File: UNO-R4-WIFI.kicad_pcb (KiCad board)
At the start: 4 copper layers, 68.6 x 53.3 mm, 266 parts, among them IC1 NLASB3157DFT2G, IC3 ISL854102FRZ-T, IC4 SGM2205-3.3XKC3G/TR, J1 TSW-103-07-G-S, J2 SSQ-110-01-G-S, J3 PH2-06-UA, J4 SSQ-108-01-G-S, J5 SSQ-115-01-G-S, J6 SM04B-SRSS-TB(LF)(SN), J7 USB_C_Receptacle_USB2.0_16P, J8 19TW-746, J9 PH2-06-UA, M1 ESP32-S2-MINI-1, P400_SCL1 CMP-018-0004-A.4, P401_SDA1 CMP-018-0004-A.4, Q1 2N7002KT1G, Q2 2N7002KT1G, Q3 2N7002KT1G, U1 R7FA4M1AB3CFM#AA0, U2 TXB0108DQSR, U6 NLASB3157DFT2G

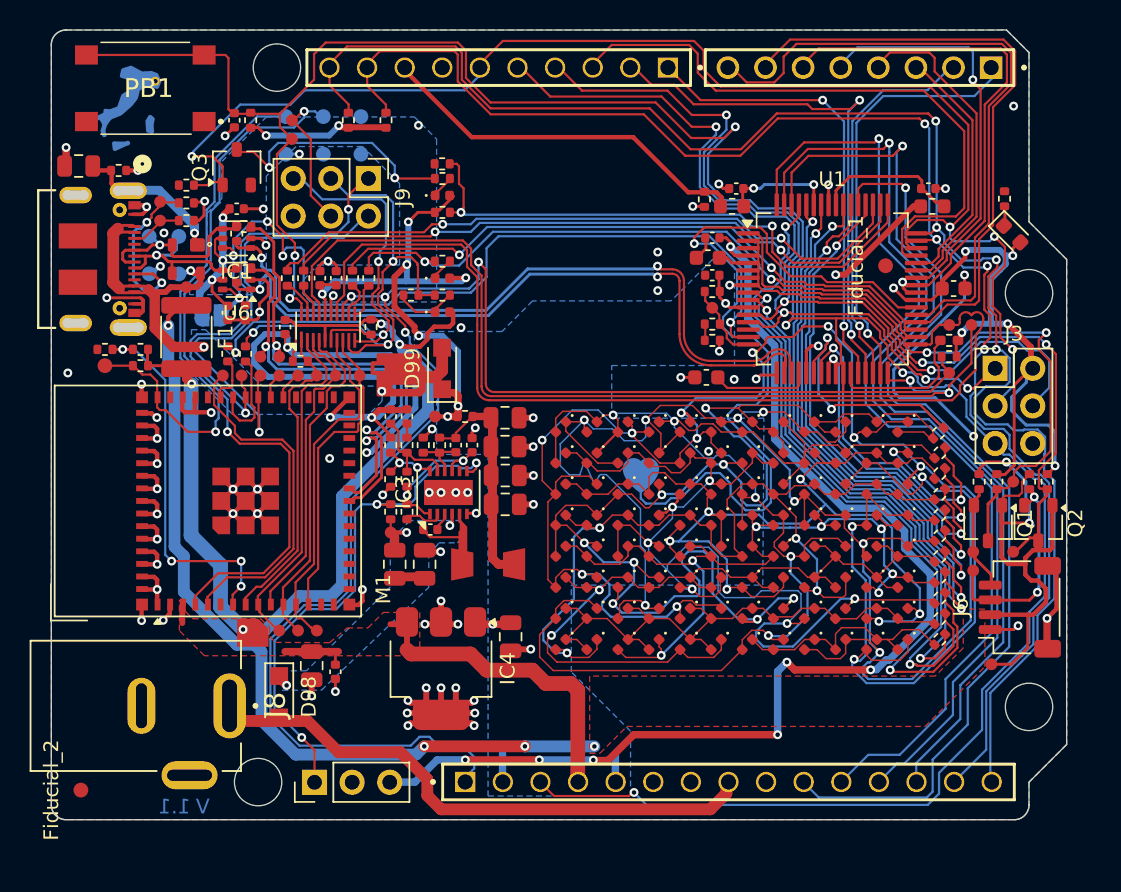
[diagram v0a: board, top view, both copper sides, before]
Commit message: silkscreen update + ESP32 footprint update
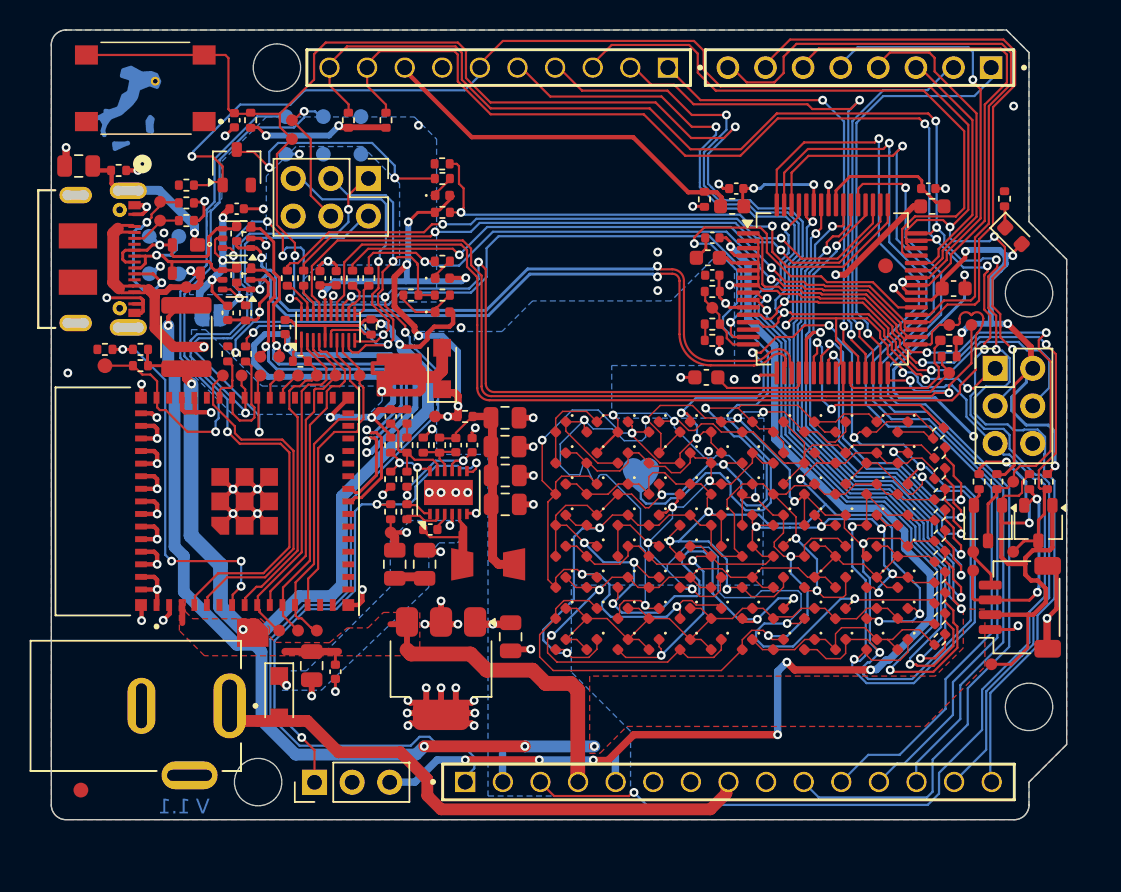
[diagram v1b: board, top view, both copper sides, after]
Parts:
- M1: value ESP32-S2-MINI-1 -> ESP32-S3-MINI-1-N8; footprint RF_Module:ESP32-S2-MINI-1 -> external_footprints:ESP32-S3-MINI-1-N8
- moved M1 2.48 mm to (127.3, 110.2)
- moved DL3 0.15 mm to (179.2, 92.2)
- renumbered U6 to IC2, PB1 to SW1
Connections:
- D98 pad 1: (no net) -> Net-(D98-K)
- D98 pad 2: (no net) -> VIN
- M1 pad 61: (no net) -> GND
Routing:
- net +5V: track 130.6 -> 131.9 mm
- net /P206: track 16.7 -> 15.5 mm
- net (no net): track 1.08 -> 0.00 mm, vias 1 -> 0
- net Net-(D98-K): track 4.31 -> 5.38 mm, vias 2 -> 3
- net /P205: track 22.2 -> 23.0 mm
- net /P204: track 21.1 -> 21.6 mm

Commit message: layer update
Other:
- rule pad_to_mask_clearance: 0.05 -> 0
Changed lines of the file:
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@@
 	(paper "A4")
 	(layers
-		(0 "F.Cu" signal "TOP")
-		(1 "In1.Cu" signal "GND")
-		(2 "In2.Cu" signal "SIG")
-		(31 "B.Cu" signal "BOTTOM")
+		(0 "F.Cu" signal)
+		(1 "In1.Cu" signal)
+		(2 "In2.Cu" signal)
+		(31 "B.Cu" signal)
 		(32 "B.Adhes" user "B.Adhesive")
 		(33 "F.Adhes" user "F.Adhesive")
-		(34 "B.Paste" user "Bottom Paste")
-		(35 "F.Paste" user "Top Paste")
-		(36 "B.SilkS" user "Bottom Overlay")
-		(37 "F.SilkS" user "Top Overlay")
-		(38 "B.Mask" user "Bottom Solder")
-		(39 "F.Mask" user "Top Solder")
-		(40 "Dwgs.User" user "Bottom Assembly")
+		(34 "B.Paste" user)
+		(35 "F.Paste" user)
+		(36 "B.SilkS" user "B.Silkscreen")
+		(37 "F.SilkS" user "F.Silkscreen")
+		(38 "B.Mask" user)
+		(39 "F.Mask" user)
+		(40 "Dwgs.User" user "User.Drawings")
 		(41 "Cmts.User" user "User.Comments")
 		(42 "Eco1.User" user "User.Eco1")
-		(43 "Eco2.User" user "Mechanical 11")
+		(43 "Eco2.User" user "User.Eco2")
 		(44 "Edge.Cuts" user)
 		(45 "Margin" user)
 		(46 "B.CrtYd" user "B.Courtyard")
 		(47 "F.CrtYd" user "F.Courtyard")
-		(48 "B.Fab" user "Top Assembly")
-		(49 "F.Fab" user "Mechanical 12")
-		(50 "User.1" user "Top 3D Body")
-		(51 "User.2" user "Top Designator")
-		(52 "User.3" user "Route Tool Path")
-		(53 "User.4" user "Board")
-		(54 "User.5" user "Assembly Notes")
-		(55 "User.6" user "Bottom Courtyard")
-		(56 "User.7" user "Mechanical 7")
-		(57 "User.8" user "Bottom 3D Body")
-		(58 "User.9" user "Mechanical 9")
+		(48 "B.Fab" user)
+		(49 "F.Fab" user)
+		(50 "User.1" user)
+		(51 "User.2" user)
+		(52 "User.3" user)
+		(53 "User.4" user)
+		(54 "User.5" user)
+		(55 "User.6" user)
+		(56 "User.7" user)
+		(57 "User.8" user)
+		(58 "User.9" user)
 	)
 	(setup
@@
 			)
 			(layer "dielectric 1"
-				(type "core")
+				(type "prepreg")
 				(color "FR4 natural")
-				(thickness 0.48)
+				(thickness 0.1)
 				(material "FR4")
 				(epsilon_r 4.5)
@@
 			)
 			(layer "dielectric 2"
-				(type "prepreg")
+				(type "core")
 				(color "FR4 natural")
-				(thickness 0.48)
+				(thickness 1.24)
 				(material "FR4")
 				(epsilon_r 4.5)
@@
 			)
 			(layer "dielectric 3"
-				(type "core")
+				(type "prepreg")
 				(color "FR4 natural")
-				(thickness 0.48)
+				(thickness 0.1)
 				(material "FR4")
 				(epsilon_r 4.5)
@@
 			(dielectric_constraints no)
 		)
-		(pad_to_mask_clearance 0.05)
+		(pad_to_mask_clearance 0)
 		(allow_soldermask_bridges_in_footprints no)
 		(aux_axis_origin 114.21111 131.67359)

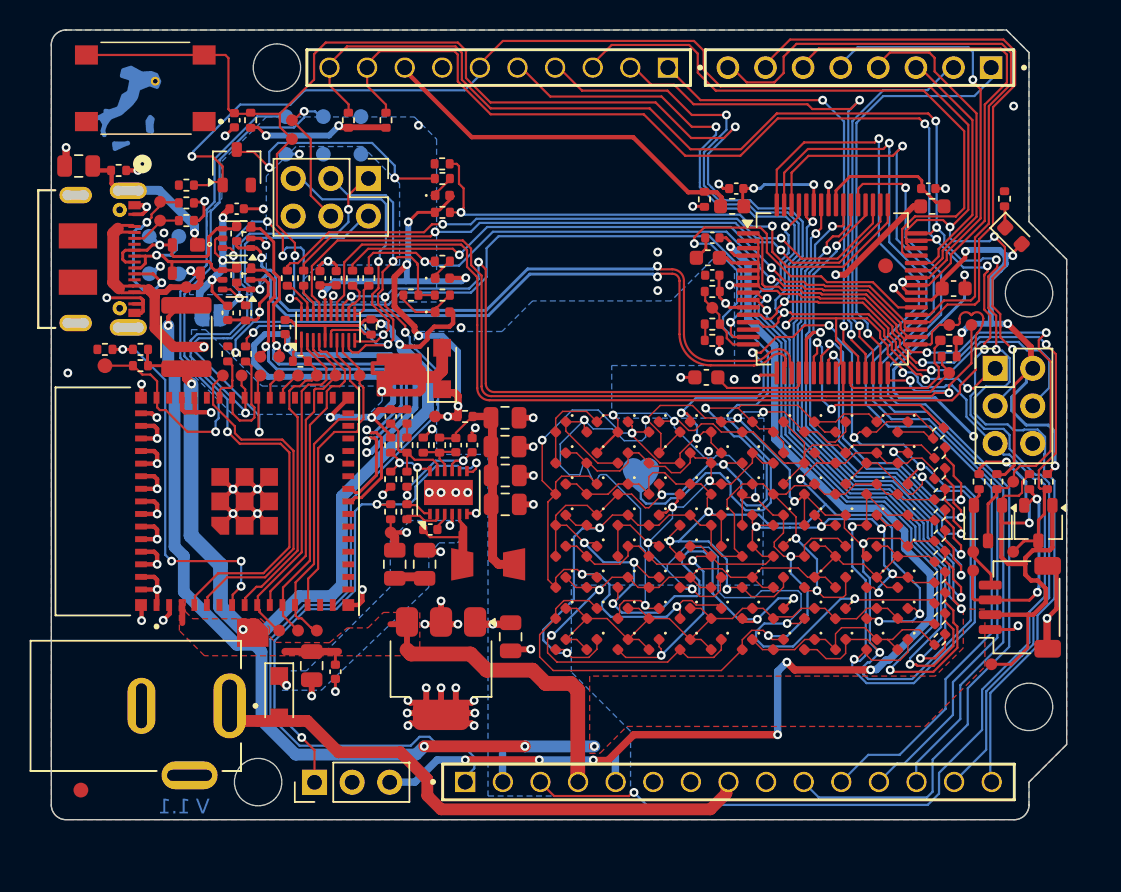
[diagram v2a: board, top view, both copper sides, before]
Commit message: no more update PCB from schematic errors
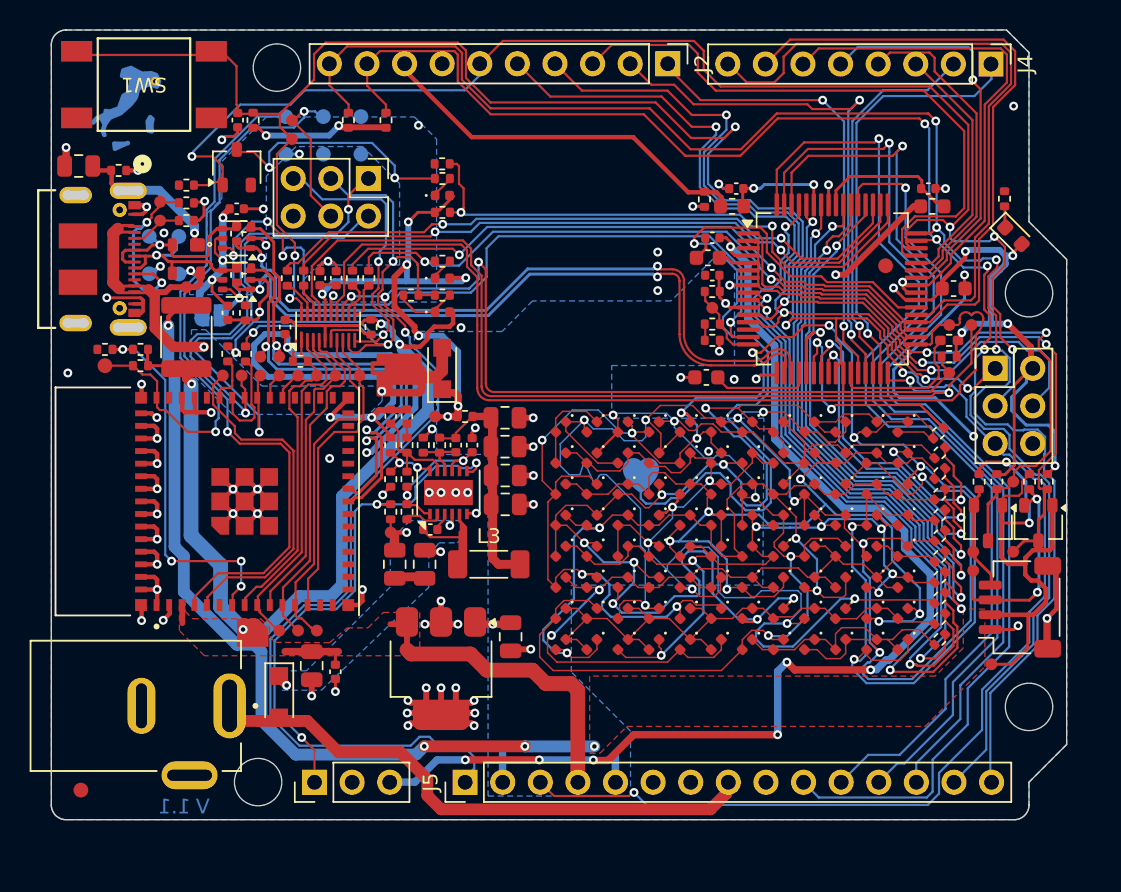
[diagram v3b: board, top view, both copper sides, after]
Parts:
- J2: footprint external_footprints:SAMTEC_SSQ-110-01-G-S -> Connector_PinHeader_2.54mm:PinHeader_1x10_P2.54mm_Vertical
- J4: footprint external_footprints:SAMTEC_SSQ-108-01-G-S -> Connector_PinHeader_2.54mm:PinHeader_1x08_P2.54mm_Vertical
- J5: footprint external_footprints:SAMTEC_SSQ-115-01-G-S -> Connector_PinHeader_2.54mm:PinHeader_1x15_P2.54mm_Vertical
- L3: footprint Vault:PMF42 -> Inductor_SMD:L_1806_4516Metric
- SW1: footprint external_footprints:1010164EV -> external_footprints:SWITCH_FSM2JSMAA_TYC
- moved J5 17.8 mm to (142.2, 129.1), turned to 90 degrees
- moved J2 11.4 mm to (155.9, 80.6), turned to -90 degrees
- moved J4 8.88 mm to (177.7, 80.6), turned to -90 degrees
- moved SW1 4.89 mm to (125.0, 84.3)
- moved C1 0.22 mm to (126.8, 84.4)
- moved R3 0.16 mm to (127.8, 84.4)
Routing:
- net GND: track 193.0 -> 193.8 mm

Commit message: fixed schematic parity + silkscreen update
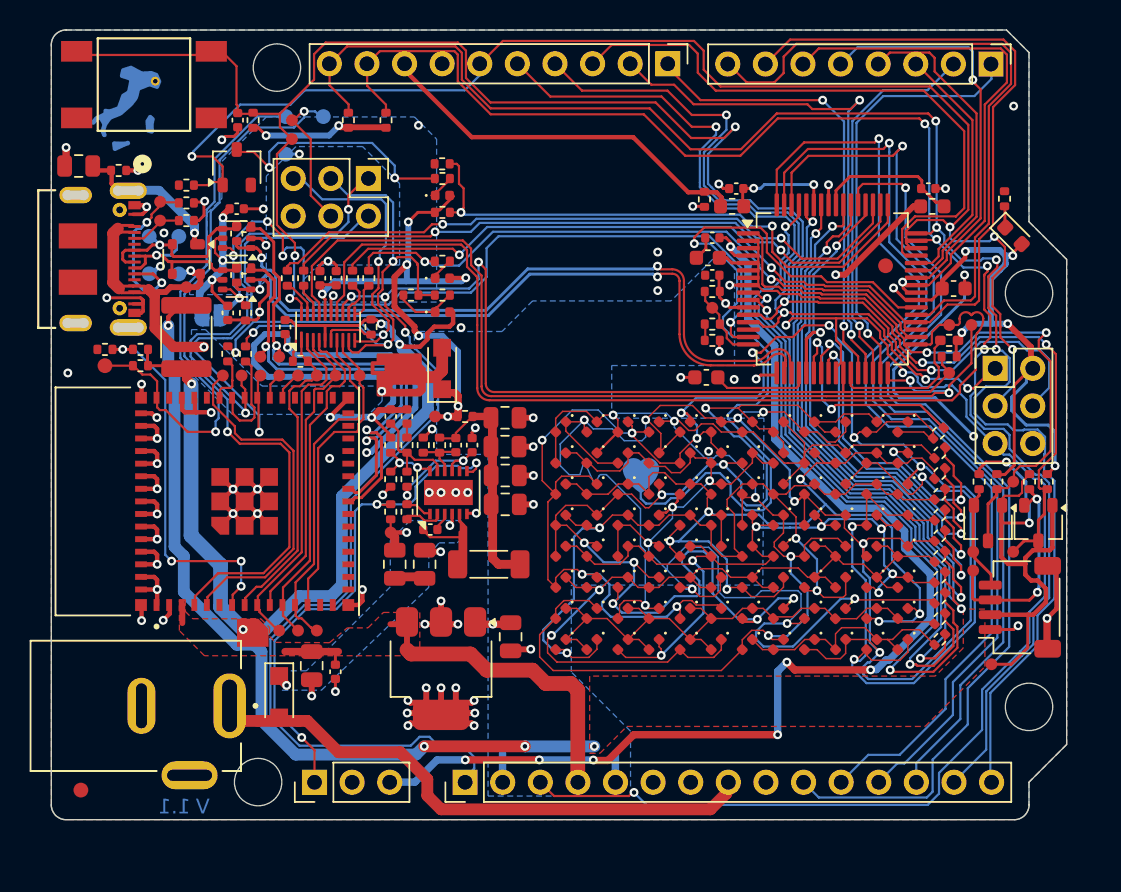
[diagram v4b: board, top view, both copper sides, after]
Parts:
- removed the ? at (135.1, 84.2)
- removed the ? at (132.6, 86.7)
- removed the ? at (135.1, 86.7)
- D97: footprint Vault:SOT190P230X110-4N -> Package_TO_SOT_SMD:SOT-143
- H1, H2, H3, H4: renamed from ?; value (none) -> MountingHole; footprint (none) -> MountingHole:MountingHole_3.2mm_M3_ISO7380
- turned D97 to -90 degrees

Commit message: fixed DRC errors + microcontroller footprint pad size update
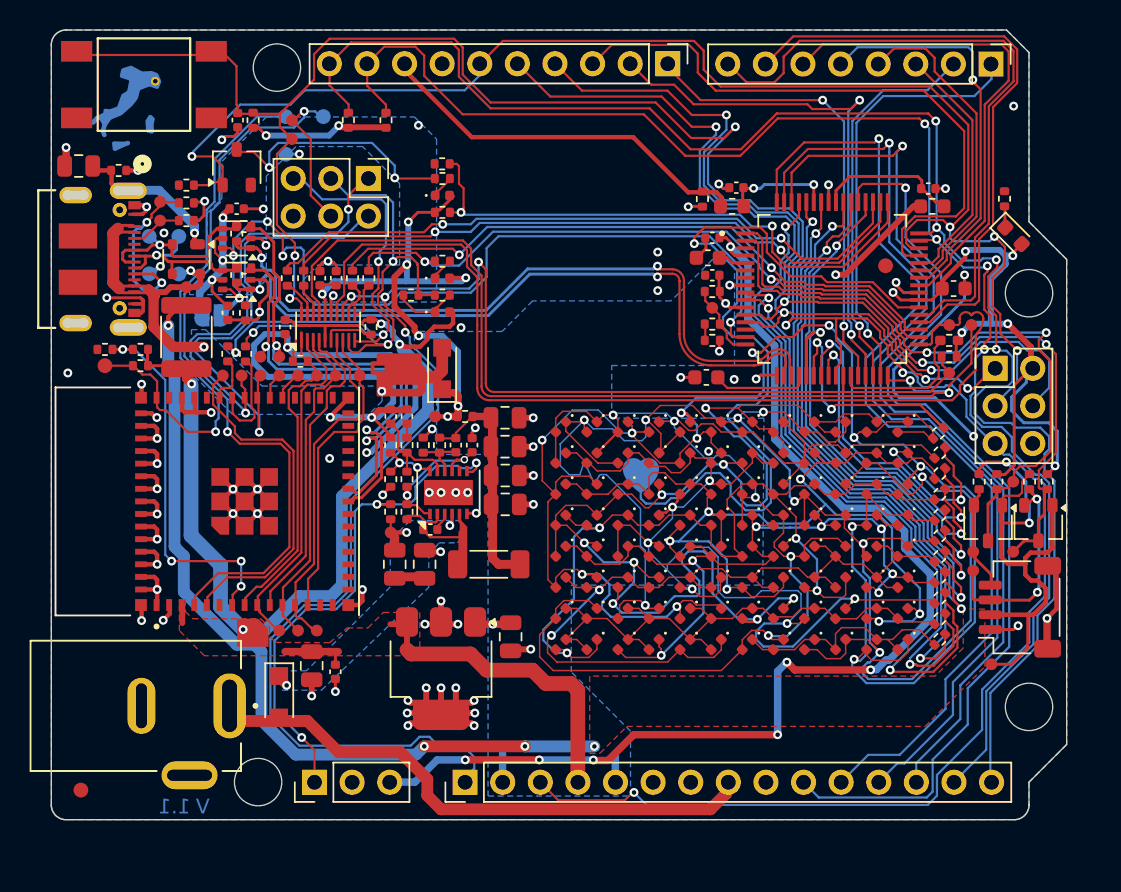
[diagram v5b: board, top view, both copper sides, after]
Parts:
- U1: footprint Package_QFP:LQFP-64_10x10mm_P0.5mm -> external_footprints:QFP50P1200X1200X170-64N
- moved R6 0.14 mm to (158.2, 89.8)
- moved C7 0.06 mm to (160.5, 89.0)
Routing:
- net /P100_AN22_SCL: track 108.2 -> 109.2 mm
- net /P107_GPT0_A: track 32.8 -> 33.3 mm
